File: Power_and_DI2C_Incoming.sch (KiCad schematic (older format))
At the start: 43 parts, among them IC1 PCA9615DPJ, J8 8P8C, Q1 BSS138, Q2 BSS138, U1 LM1117-3.3, U3 LM2676SX-5.0, U4 LM2676SX-12

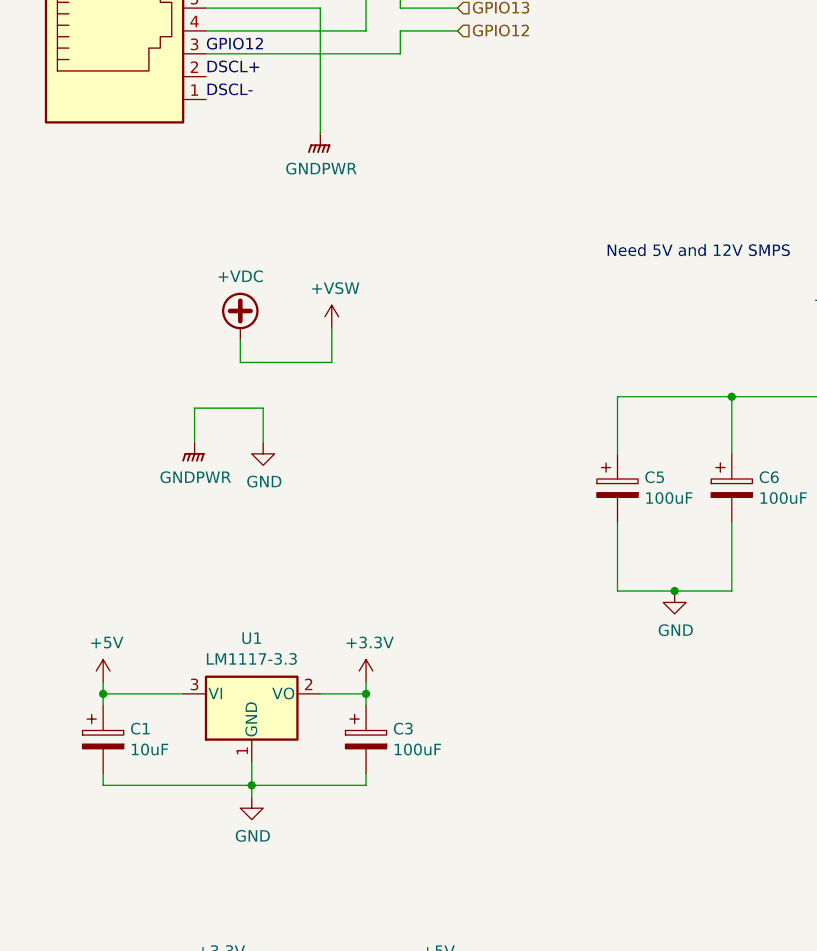
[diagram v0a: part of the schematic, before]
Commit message: Updated Schematic to correct power page
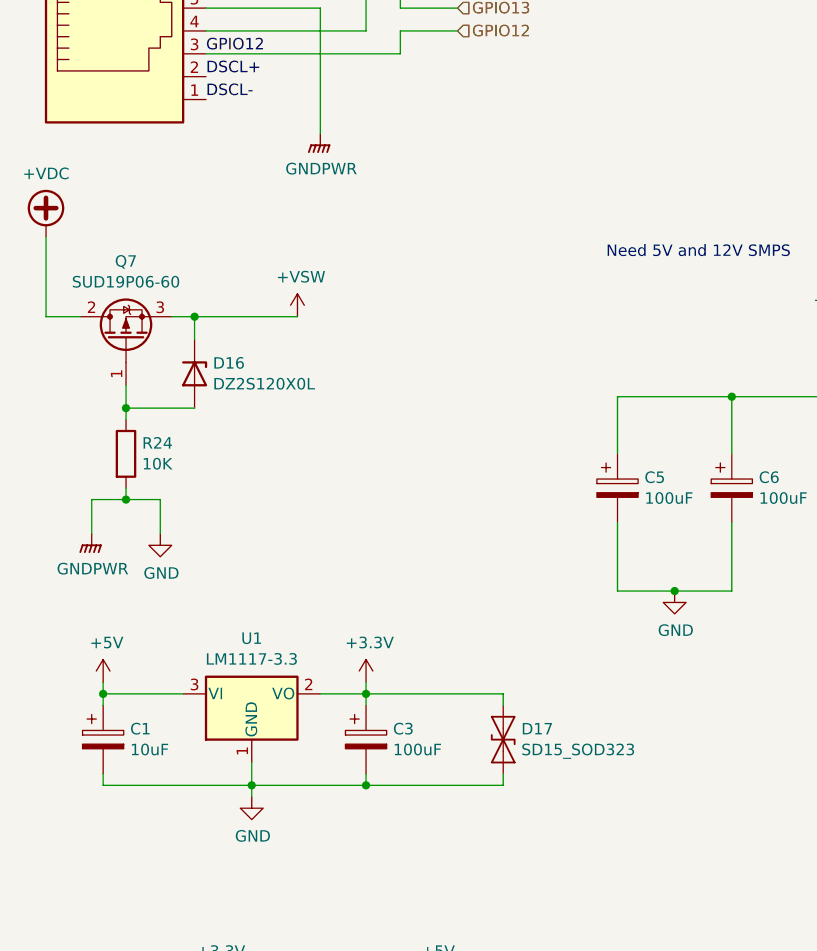
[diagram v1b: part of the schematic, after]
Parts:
- added D16: DZ2S120X0L, Diode_SMD:D_SOD-523, symbol Diode:DZ2S120X0L
- added D17: SD15_SOD323, Diode_SMD:D_SOD-323, symbol Diode:SD15_SOD323
- added Q7: SUD19P06-60, Package_TO_SOT_SMD:TO-252-2, symbol Transistor_FET:SUD19P06-60
- added R24: 10K, Resistor_SMD:R_0603_1608Metric, symbol Device:R
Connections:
- wire segments 116 -> 127
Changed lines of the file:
@@
 L power:GND #PWR021
 U 1 1 5FBB8F95
-P 1850 3250
-F 0 "#PWR021" H 1850 3000 50  0001 C CNN
-F 1 "GND" H 1855 3077 50  0000 C CNN
-F 2 "" H 1850 3250 50  0001 C CNN
-F 3 "" H 1850 3250 50  0001 C CNN
-	1    1850 3250
-	1    0    0    -1
-$EndComp
-Wire Wire Line
-	1850 3100 1850 3250
+P 1400 3650
+F 0 "#PWR021" H 1400 3400 50  0001 C CNN
+F 1 "GND" H 1405 3477 50  0000 C CNN
+F 2 "" H 1400 3650 50  0001 C CNN
+F 3 "" H 1400 3650 50  0001 C CNN
+	1    1400 3650
+	1    0    0    -1
+$EndComp
+Wire Wire Line
+	1400 3500 1400 3650
 $Comp
 L power:+VSW #PWR023
 U 1 1 5FBBBB47
-P 2150 2750
-F 0 "#PWR023" H 2150 2600 50  0001 C CNN
-F 1 "+VSW" H 2165 2923 50  0000 C CNN
-F 2 "" H 2150 2750 50  0001 C CNN
-F 3 "" H 2150 2750 50  0001 C CNN
-	1    2150 2750
-	1    0    0    -1
-$EndComp
-Wire Wire Line
-	1750 2900 2150 2900
-Wire Wire Line
-	2150 2900 2150 2750
+P 2000 2700
+F 0 "#PWR023" H 2000 2550 50  0001 C CNN
+F 1 "+VSW" H 2015 2873 50  0000 C CNN
+F 2 "" H 2000 2700 50  0001 C CNN
+F 3 "" H 2000 2700 50  0001 C CNN
+	1    2000 2700
+	1    0    0    -1
+$EndComp
 Wire Wire Line
 	2450 1550 2450 1450
@@
 L power:+VDC #PWR018
 U 1 1 5FEACF27
-P 1750 2800
-F 0 "#PWR018" H 1750 2700 50  0001 C CNN
-F 1 "+VDC" H 1750 3075 50  0000 C CNN
-F 2 "" H 1750 2800 50  0001 C CNN
-F 3 "" H 1750 2800 50  0001 C CNN
-	1    1750 2800
-	1    0    0    -1
-$EndComp
-Wire Wire Line
-	1750 2800 1750 2900
+P 900 2350
+F 0 "#PWR018" H 900 2250 50  0001 C CNN
+F 1 "+VDC" H 900 2625 50  0000 C CNN
+F 2 "" H 900 2350 50  0001 C CNN
+F 3 "" H 900 2350 50  0001 C CNN
+	1    900  2350
+	1    0    0    -1
+$EndComp
 $Comp
 L power:GNDPWR #PWR017
 U 1 1 5FEB2DCE
-P 1550 3250
-F 0 "#PWR017" H 1550 3050 50  0001 C CNN
-F 1 "GNDPWR" H 1554 3096 50  0000 C CNN
-F 2 "" H 1550 3200 50  0001 C CNN
-F 3 "" H 1550 3200 50  0001 C CNN
-	1    1550 3250
-	1    0    0    -1
-$EndComp
-Wire Wire Line
-	1550 3250 1550 3100
-Wire Wire Line
-	1550 3100 1850 3100
+P 1100 3650
+F 0 "#PWR017" H 1100 3450 50  0001 C CNN
+F 1 "GNDPWR" H 1104 3496 50  0000 C CNN
+F 2 "" H 1100 3600 50  0001 C CNN
+F 3 "" H 1100 3600 50  0001 C CNN
+	1    1100 3650
+	1    0    0    -1
+$EndComp
+Wire Wire Line
+	1100 3650 1100 3500
 $Comp
 L Device:CP C1
@@
 	1    0    0    -1
 $EndComp
+$Comp
+L Transistor_FET:SUD19P06-60 Q7
+U 1 1 6018C1D6
+P 1250 2800
+F 0 "Q7" V 1592 2800 50  0000 C CNN
+F 1 "SUD19P06-60" V 1501 2800 50  0000 C CNN
+F 2 "Package_TO_SOT_SMD:TO-252-2" H 1445 2725 50  0001 L CIN
+F 3 "https://www.vishay.com/docs/69253/sud19p06.pdf" H 1250 2800 50  0001 C CNN
+	1    1250 2800
+	0    -1   -1   0
+$EndComp
+Wire Wire Line
+	1100 3500 1250 3500
+$Comp
+L Diode:DZ2S120X0L D16
+U 1 1 601A1271
+P 1550 2950
+F 0 "D16" V 1504 3030 50  0000 L CNN
+F 1 "DZ2S120X0L" V 1595 3030 50  0000 L CNN
+F 2 "Diode_SMD:D_SOD-523" H 1550 2775 50  0001 C CNN
+F 3 "https://industrial.panasonic.com/content/data/SC/ds/ds4/DZ2S12000L_E.pdf" H 1550 2950 50  0001 C CNN
+	1    1550 2950
+	0    1    1    0
+$EndComp
+$Comp
+L Device:R R24
+U 1 1 601A404D
+P 1250 3300
+F 0 "R24" H 1320 3346 50  0000 L CNN
+F 1 "10K" H 1320 3255 50  0000 L CNN
+F 2 "Resistor_SMD:R_0603_1608Metric" V 1180 3300 50  0001 C CNN
+F 3 "~" H 1250 3300 50  0001 C CNN
+F 4 "ERJ-3GEYJ103V" H 1250 3300 50  0001 C CNN "MFG Part"
+F 5 "Panasonic Electronic Components" H 1250 3300 50  0001 C CNN "MFG Name"
+	1    1250 3300
+	1    0    0    -1
+$EndComp
+Wire Wire Line
+	1550 3100 1250 3100
+Wire Wire Line
+	1250 3000 1250 3100
+Connection ~ 1250 3100
+Wire Wire Line
+	1250 3100 1250 3150
+Wire Wire Line
+	1250 3450 1250 3500
+Connection ~ 1250 3500
+Wire Wire Line
+	1250 3500 1400 3500
+Wire Wire Line
+	900  2700 1050 2700
+Wire Wire Line
+	900  2350 900  2700
+Wire Wire Line
+	1450 2700 1550 2700
+Wire Wire Line
+	1550 2800 1550 2700
+Connection ~ 1550 2700
+Wire Wire Line
+	1550 2700 2000 2700
+$Comp
+L Diode:SD15_SOD323 D17
+U 1 1 601D8AAE
+P 2900 4550
+F 0 "D17" V 2854 4629 50  0000 L CNN
+F 1 "SD15_SOD323" V 2945 4629 50  0000 L CNN
+F 2 "Diode_SMD:D_SOD-323" H 2900 4350 50  0001 C CNN
+F 3 "https://www.littelfuse.com/~/media/electronics/datasheets/tvs_diode_arrays/littelfuse_tvs_diode_array_sd_c_datasheet.pdf.pdf" H 2900 4550 50  0001 C CNN
+	1    2900 4550
+	0    1    1    0
+$EndComp
+Wire Wire Line
+	2300 4350 2900 4350
+Wire Wire Line
+	2900 4350 2900 4400
+Wire Wire Line
+	2900 4700 2900 4750
+Wire Wire Line
+	2900 4750 2300 4750
+Connection ~ 2300 4750
 $EndSCHEMATC
